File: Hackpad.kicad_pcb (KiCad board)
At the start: 2 copper layers, 11 parts, among them SW1 SW_Push, SW2 SW_Push, SW3 SW_Push, SW4 SW_Push, SW5 RotaryEncoder, U1 XIAO-RP2040-DIP, U2 SSD1306

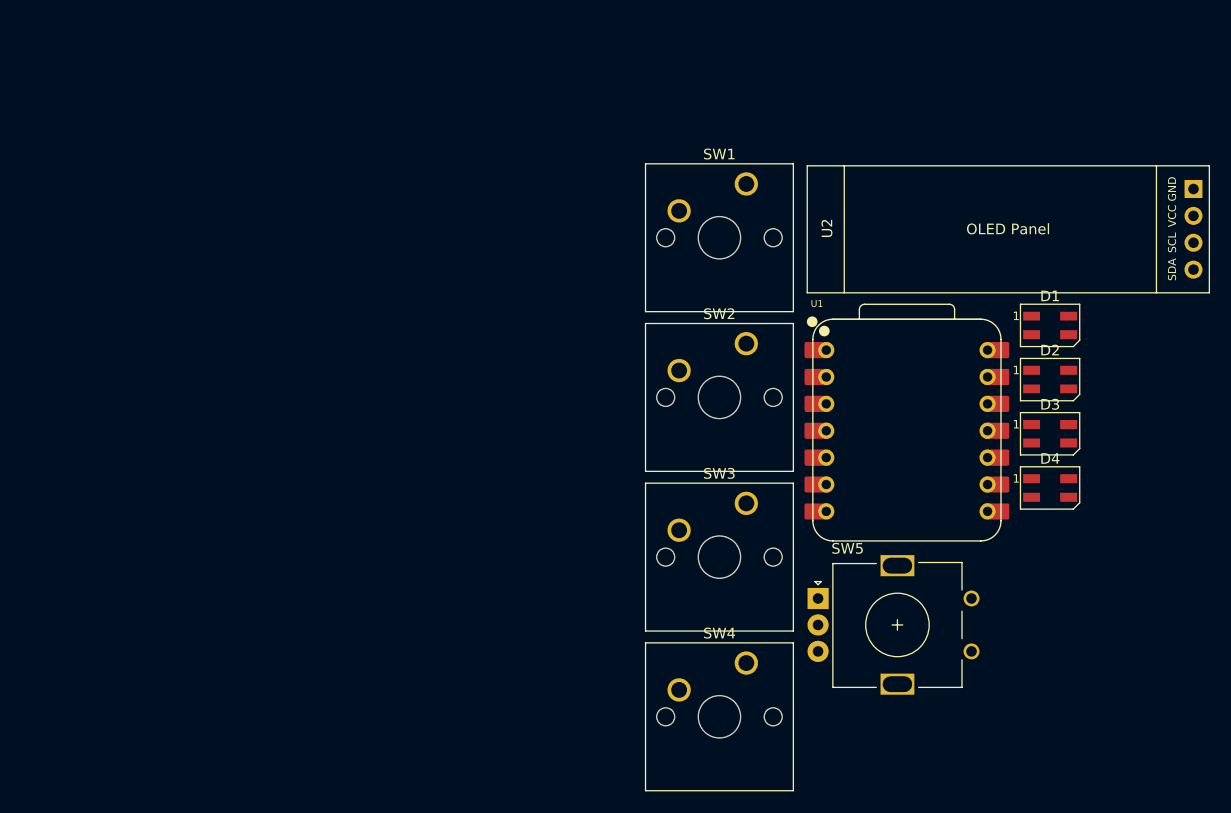
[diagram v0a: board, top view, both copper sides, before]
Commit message: Routed PCB
Routed PCB and finished overall PCB construction
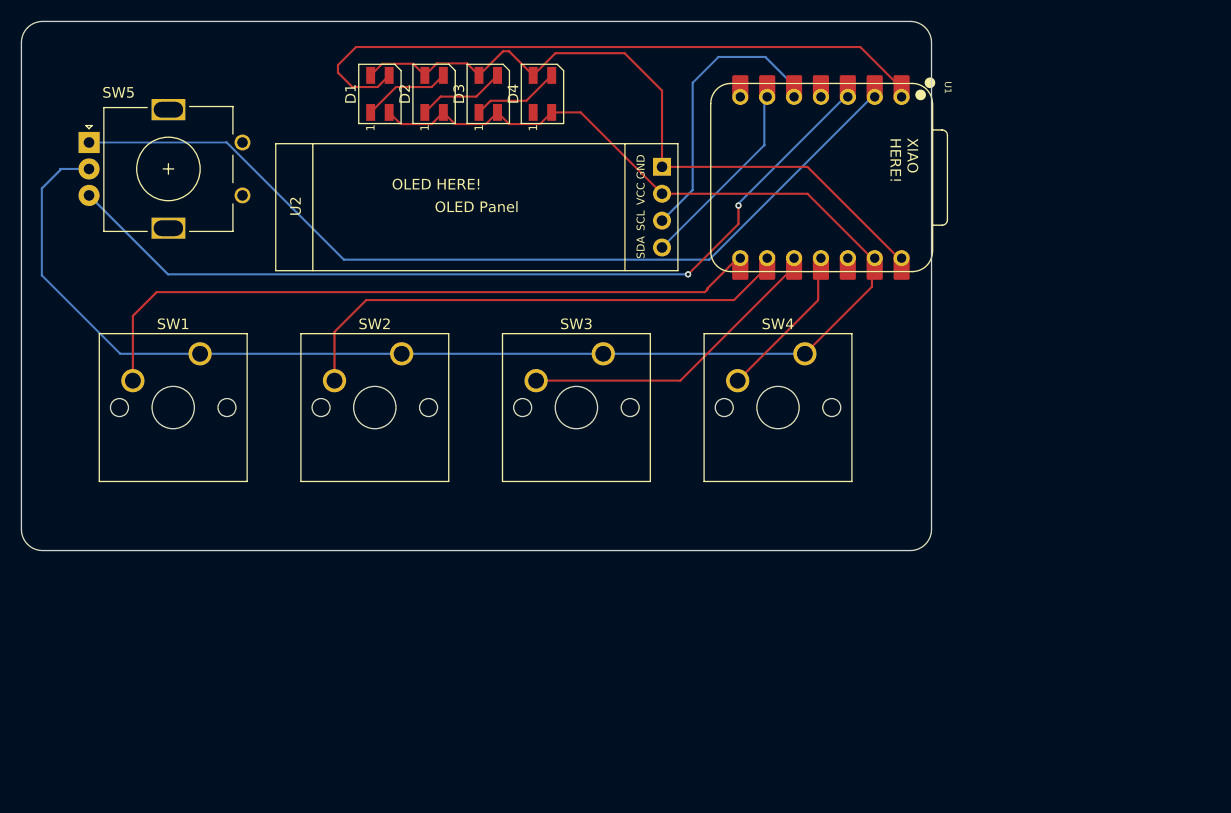
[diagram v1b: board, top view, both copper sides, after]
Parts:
- moved SW5 81.3 mm to (75.4, 65.4)
- moved D1 67.0 mm to (102.9, 60.9), turned to 90 degrees
- moved D2 64.2 mm to (108.0, 60.9), turned to 90 degrees
- moved D3 62.0 mm to (113.1, 60.9), turned to 90 degrees
- moved D4 60.7 mm to (118.2, 60.9), turned to 90 degrees
- moved SW1 54.1 mm to (85.9, 85.4)
- moved U2 50.3 mm to (93.0, 65.6)
- moved SW2 32.6 mm to (104.9, 85.4)
- moved SW4 29.7 mm to (143.0, 85.4)
- moved U1 25.3 mm to (144.6, 68.8), turned to -90 degrees
- moved SW3 19.6 mm to (124.0, 85.4)
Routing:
- net GND: track 0.00 -> 154.4 mm
- net Net-(U1-GPIO27/ADC1/A1): track 0.00 -> 84.9 mm
- net Net-(U1-GPIO28/ADC2/A2): track 0.00 -> 82.6 mm, vias 0 -> 2
- net +5V: track 0.00 -> 66.8 mm
- net Net-(U1-GPIO1/RX): track 0.00 -> 65.6 mm
- net Net-(D1-DIN): track 0.00 -> 62.9 mm
- net Net-(U1-GPIO2/SCK): track 0.00 -> 48.8 mm
- net Net-(U1-GPIO4/MISO): track 0.00 -> 29.5 mm
- net Net-(U1-GPIO6/SDA): track 0.00 -> 26.9 mm
- net Net-(U1-GPIO7/SCL): track 0.00 -> 18.2 mm
- net Net-(U1-GPIO3/MOSI): track 0.00 -> 14.7 mm
- net Net-(D3-DOUT): track 0.00 -> 8.32 mm
- net Net-(D1-DOUT): track 0.00 -> 8.32 mm
- net Net-(D2-DOUT): track 0.00 -> 8.32 mm
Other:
- board outline added: 86 x 50 mm
- board text added: "OLED HERE!"
- board text added: "XIAO HERE!"
